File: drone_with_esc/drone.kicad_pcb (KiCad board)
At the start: 2 copper layers, 50.8 x 50.8 mm, 47 parts, among them J1 Conn_01x06, J2 Conn_01x02, J3 Conn_01x02, J4 Conn_01x02, J5 Conn_01x02, J6 Conn_01x02, Q1 Si2319CDS, Q2 Si2319CDS, Q3 Si2319CDS, Q4 Si2319CDS, SW1 SW_Push_Open, SW2 SW_Push_Open, U1 ESP32-WROOM-32, U2 MPU-6050, U3 DWM1000, U4 BMP280, U5 TPS63001

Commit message: update new drone format
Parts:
- removed D1, D2, D3, D4: 1N5819, Diode_THT:D_DO-41_SOD81_P10.16mm_Horizontal
- removed J3, J4, J5, J6: Conn_01x02, Connector_PinHeader_2.54mm:PinHeader_1x02_P2.54mm_Vertical
- removed L1: LPS4012-103MRB, LPS4012:IND_LPS4012-103MRB
- removed Q1, Q2, Q3, Q4: Si2319CDS, Package_TO_SOT_SMD:SOT-23
- removed R11: 100, Resistor_SMD:R_0603_1608Metric
- removed R14, R15, R16, R17, R3, R4, R5, R6: R_Small, Resistor_SMD:R_0603_1608Metric
- C4, C5, C7: value 0.1uF -> C
- J2: value Conn_01x02 -> Conn_01x06; footprint Connector_PinHeader_2.54mm:PinHeader_1x02_P2.54mm_Vertical -> Connector_PinHeader_2.54mm:PinHeader_1x06_P2.54mm_Vertical
- U5: value TPS63001 -> LM317_SOT-223; footprint Package_SON:Texas_DRC0010J_ThermalVias -> Package_TO_SOT_SMD:SOT-223-3_TabPin2
- moved C4 46.5 mm to (115.1, 76.4)
- moved C5 44.2 mm to (111.5, 75.4), turned to 0 degrees
- moved C7 43.5 mm to (108.8, 73.8), turned to 0 degrees
- moved U5 41.6 mm to (110.2, 80.9), turned to -90 degrees
- moved J2 13.1 mm to (94.4, 114.3)
- moved C3 5.94 mm to (102.8, 97.4)
- moved C6 5.94 mm to (101.2, 110.4)
- moved D5 5.94 mm to (74.7, 98.0)
- moved J1 5.94 mm to (103.8, 75.8)
- moved R1 5.94 mm to (103.1, 103.0)
- moved R13 5.94 mm to (87.2, 109.5)
- moved R2 5.94 mm to (100.9, 103.0)
- moved R7 5.94 mm to (96.0, 108.6)
- moved C1 5.94 mm to (101.2, 97.4)
- moved C2 5.94 mm to (97.4, 101.2)
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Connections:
- C4 pad 1: Net-(C4-Pad1) -> VCC
- C7 pad 1: VCC -> +BATT
- J2 pad 1: BAT+ -> MOTOR_1
- J2 pad 2: GND -> MOTOR_2
- U5 pad 1: VCC -> GND
- U5 pad 2: Net-(L1-Pad2) -> VCC
- U5 pad 3: GND -> +BATT
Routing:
- net BAT+: track 157.4 -> 0.00 mm, vias 1 -> 0
- net MOTOR_3: track 38.8 -> 0.00 mm, vias 2 -> 0
- net MOTOR_4: track 34.3 -> 0.51 mm, vias 2 -> 0
- net MOTOR_1: track 29.2 -> 0.00 mm, vias 2 -> 0
- net VCC: track 142.8 -> 115.0 mm, vias 4 -> 2
- net Net-(D3-Pad2): track 12.7 -> 0.00 mm
- net Net-(D1-Pad2): track 10.2 -> 0.00 mm
- net Net-(D2-Pad2): track 9.13 -> 0.00 mm
- net Net-(D4-Pad2): track 8.98 -> 0.00 mm
- net GND: track 25.5 -> 17.0 mm
- net MOTOR_2: track 8.16 -> 0.00 mm
- net Net-(C4-Pad1): track 5.83 -> 0.00 mm
- net +BATT: track 0.00 -> 4.40 mm
- net Net-(L1-Pad2): track 4.28 -> 0.00 mm
- net Net-(L1-Pad1): track 4.13 -> 0.00 mm
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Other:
- outline, holes or cut-outs redrawn

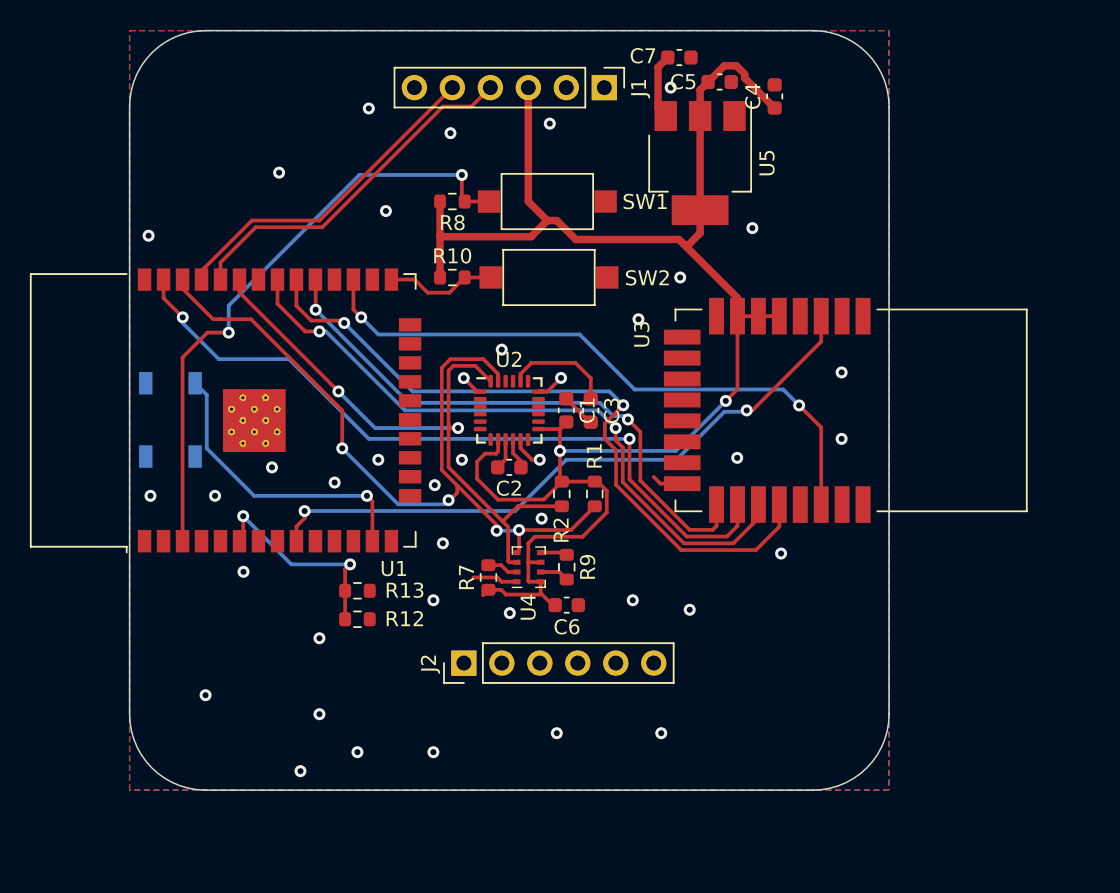
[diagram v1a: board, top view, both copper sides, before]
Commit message: add regulator
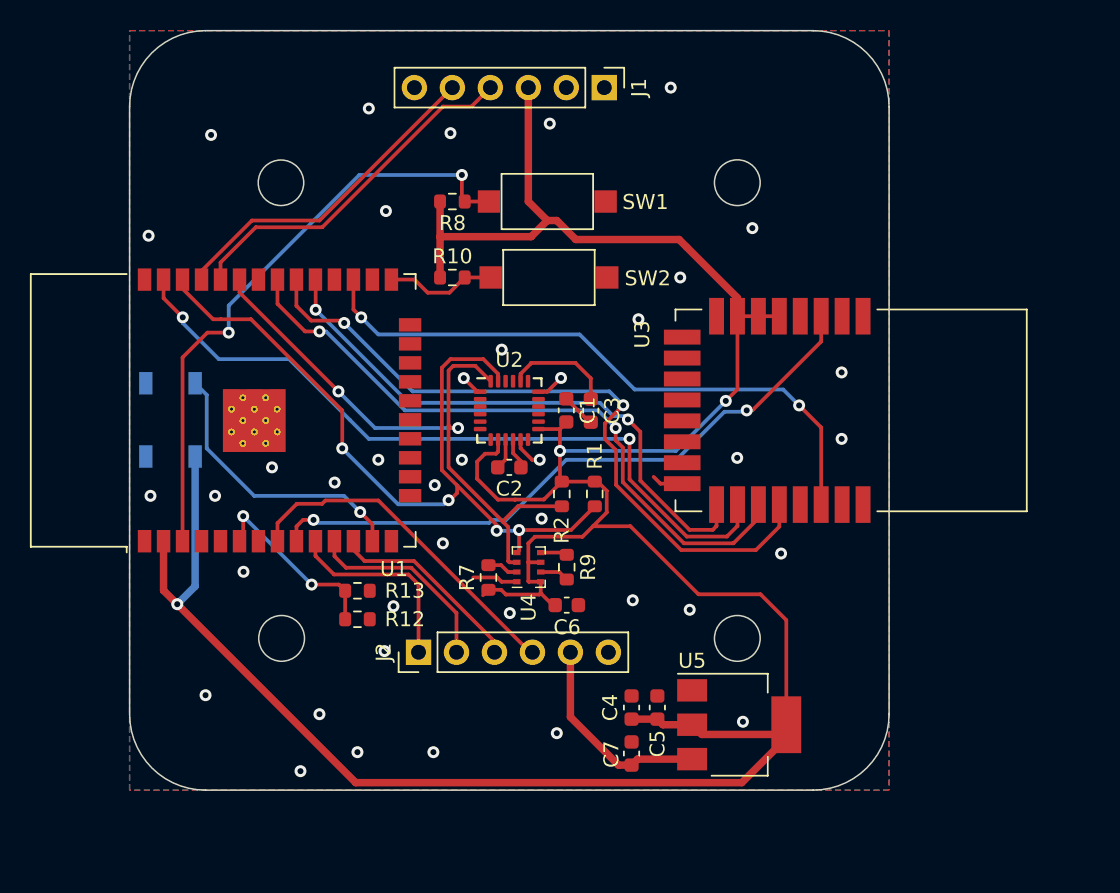
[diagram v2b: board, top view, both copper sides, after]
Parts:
- moved C7 46.7 mm to (105.6, 120.3), turned to 90 degrees
- moved C5 42.0 mm to (107.3, 117.3), turned to 90 degrees
- moved C4 42.0 mm to (105.6, 117.3)
- moved U5 37.7 mm to (112.8, 118.4), turned to 0 degrees
- moved J2 3.12 mm to (91.3, 113.6)
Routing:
- net VCC: track 115.0 -> 193.5 mm, vias 2 -> 3
- net MOTOR_4: track 0.51 -> 23.6 mm
- net MOTOR_2: track 0.00 -> 13.4 mm
- net MOTOR_3: track 0.00 -> 13.3 mm
- net MOTOR_1: track 0.00 -> 13.2 mm
- net +BATT: track 4.40 -> 14.0 mm
- net BAT_LEVEL: track 14.1 -> 12.6 mm
- net Net-(D5-DIN): track 19.9 -> 19.0 mm
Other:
- outline, holes or cut-outs redrawn
